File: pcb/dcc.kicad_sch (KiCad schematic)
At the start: 68 parts, among them U10 LM339, U11 LM339, U4 L78L05_SOT89, U5 L79L05_SOT89, U6 LM339, U7 LM339, U8 LM339, U9 4052

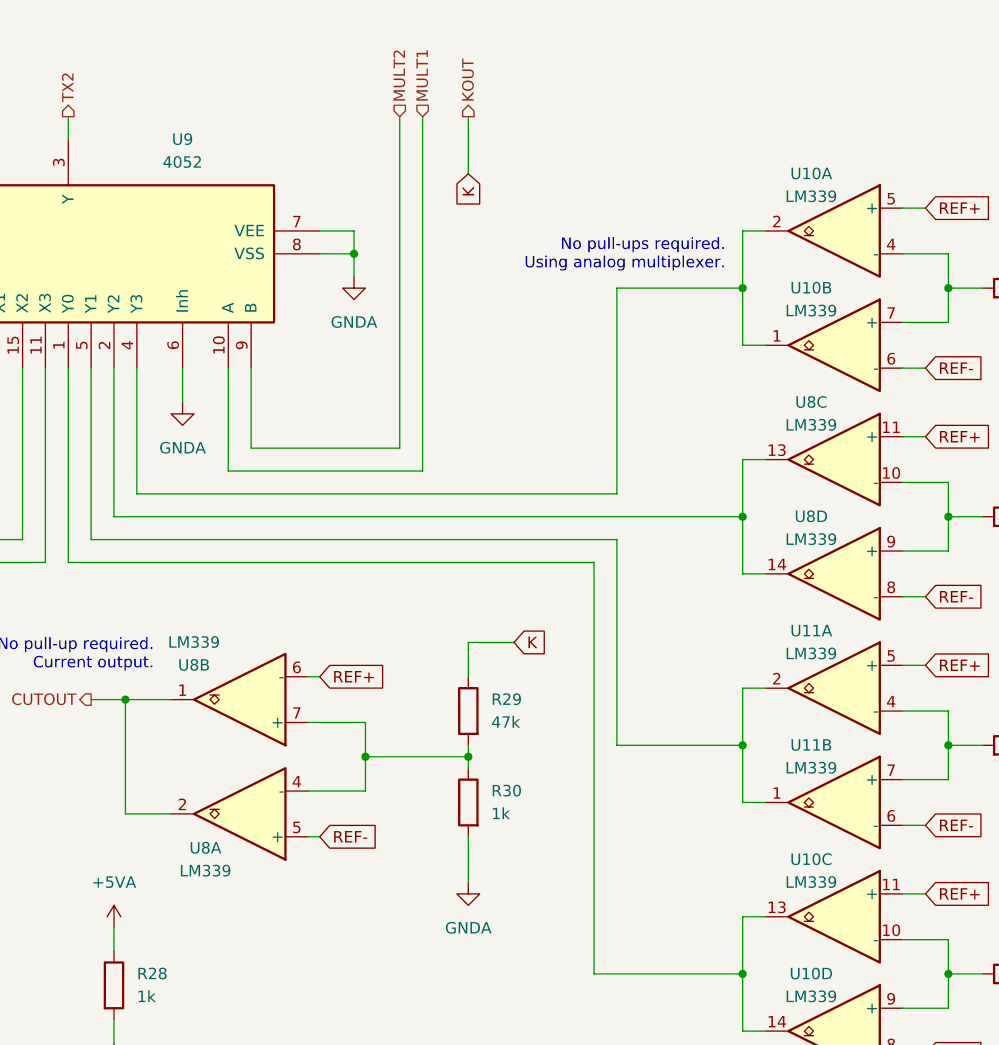
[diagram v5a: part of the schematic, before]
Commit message: pcb: wire multiplexors.
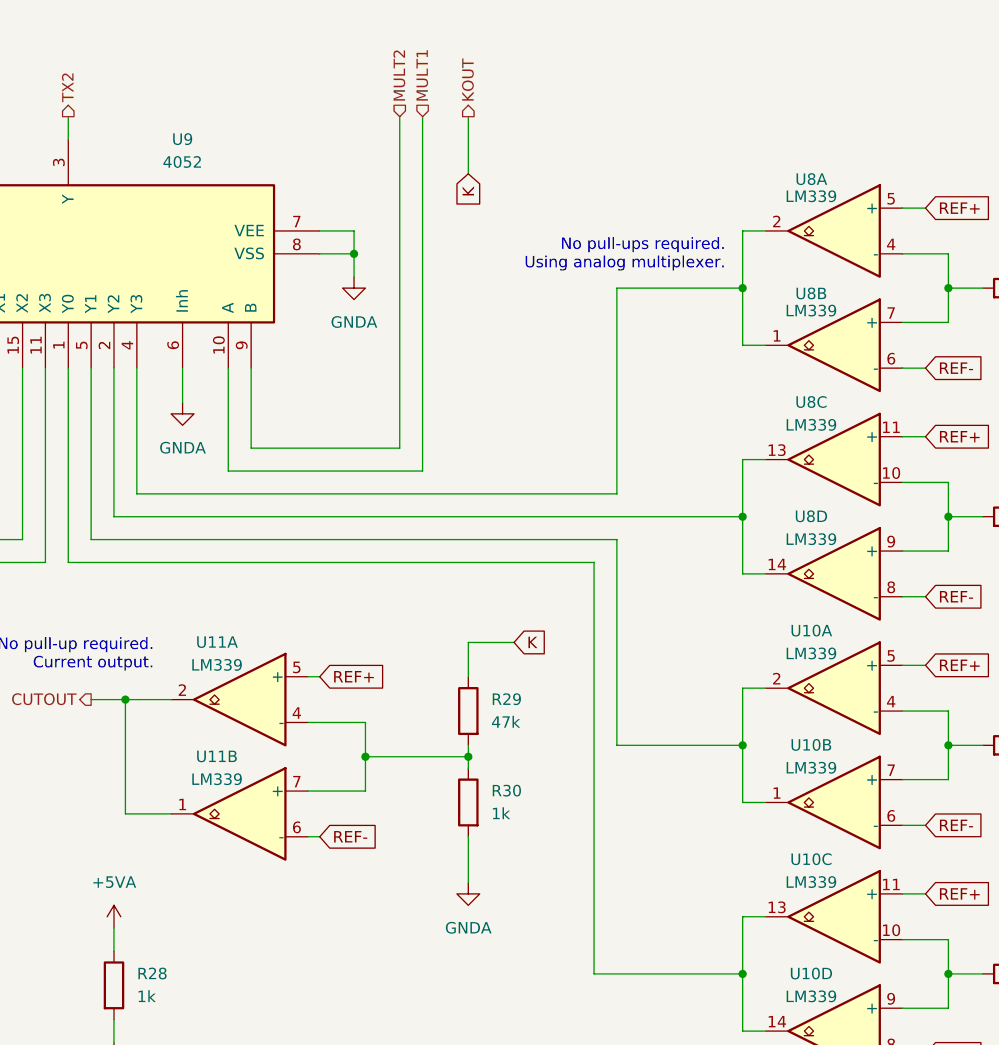
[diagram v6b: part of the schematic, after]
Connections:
- net CUTOUT: now also U11.1, U11.2; no longer U8.1, U8.2
- net REF+: now also U8.5 (+); no longer U8.6 (-)
- net REF-: now also U8.6 (-); no longer U8.5 (+)
- net at U10.1, U10.2: now also U9.5 (Y1); no longer U9.4 (Y3)
- net at U10.4 (-), U10.7 (+): now also R33.2; no longer R31.2
- net at U8.4 (-), U8.7 (+): now also R31.2; no longer R29.2, R30.1
- net at U11.4 (-), U11.7 (+): now also R29.2, R30.1; no longer R33.2
- new net: U8.1, U8.2, U9.4 (Y3)
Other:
- moved on the sheet: U10A, U10B, U11A, U11B, U8A, U8B
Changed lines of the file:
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@@
     )
   )
-  (symbol (lib_id "Comparator:LM339") (at 223.52 40.64 0) (mirror y) (unit 1)
-    (in_bom yes) (on_board yes) (dnp no)
-    (property "Reference" "U10" (at 220.98 34.29 0)
-      (effects (font (size 1.27 1.27)))
-    )
-    (property "Value" "LM339" (at 220.98 36.83 0)
-      (effects (font (size 1.27 1.27)))
-    )
-    (property "Footprint" "Package_SO:SO-14_3.9x8.65mm_P1.27mm" (at 224.79 38.1 0)
-      (effects (font (size 1.27 1.27)) hide)
-    )
-    (property "Datasheet" "https://www.st.com/resource/en/datasheet/lm139.pdf" (at 222.25 35.56 0)
+  (symbol (lib_id "Comparator:LM339") (at 223.52 91.44 0) (mirror y) (unit 1)
+    (in_bom yes) (on_board yes) (dnp no)
+    (property "Reference" "U10" (at 220.98 85.09 0)
+      (effects (font (size 1.27 1.27)))
+    )
+    (property "Value" "LM339" (at 220.98 87.63 0)
+      (effects (font (size 1.27 1.27)))
+    )
+    (property "Footprint" "Package_SO:SO-14_3.9x8.65mm_P1.27mm" (at 224.79 88.9 0)
+      (effects (font (size 1.27 1.27)) hide)
+    )
+    (property "Datasheet" "https://www.st.com/resource/en/datasheet/lm139.pdf" (at 222.25 86.36 0)
       (effects (font (size 1.27 1.27)) hide)
     )
@@
     )
   )
-  (symbol (lib_id "Comparator:LM339") (at 157.48 92.71 180) (unit 2)
-    (in_bom yes) (on_board yes) (dnp no)
-    (property "Reference" "U8" (at 152.4 88.9 0)
-      (effects (font (size 1.27 1.27)))
-    )
-    (property "Value" "LM339" (at 152.4 86.36 0)
-      (effects (font (size 1.27 1.27)))
-    )
-    (property "Footprint" "Package_SO:SO-14_3.9x8.65mm_P1.27mm" (at 158.75 95.25 0)
-      (effects (font (size 1.27 1.27)) hide)
-    )
-    (property "Datasheet" "https://www.st.com/resource/en/datasheet/lm139.pdf" (at 156.21 97.79 0)
+  (symbol (lib_id "Comparator:LM339") (at 223.52 53.34 0) (mirror y) (unit 2)
+    (in_bom yes) (on_board yes) (dnp no)
+    (property "Reference" "U8" (at 220.98 47.625 0)
+      (effects (font (size 1.27 1.27)))
+    )
+    (property "Value" "LM339" (at 220.98 49.53 0)
+      (effects (font (size 1.27 1.27)))
+    )
+    (property "Footprint" "Package_SO:SO-14_3.9x8.65mm_P1.27mm" (at 224.79 50.8 0)
+      (effects (font (size 1.27 1.27)) hide)
+    )
+    (property "Datasheet" "https://www.st.com/resource/en/datasheet/lm139.pdf" (at 222.25 48.26 0)
       (effects (font (size 1.27 1.27)) hide)
     )
@@
     )
   )
-  (symbol (lib_id "Comparator:LM339") (at 223.52 104.14 0) (mirror y) (unit 2)
-    (in_bom yes) (on_board yes) (dnp no)
-    (property "Reference" "U11" (at 220.98 97.79 0)
-      (effects (font (size 1.27 1.27)))
-    )
-    (property "Value" "LM339" (at 220.98 100.33 0)
-      (effects (font (size 1.27 1.27)))
-    )
-    (property "Footprint" "Package_SO:SO-14_3.9x8.65mm_P1.27mm" (at 224.79 101.6 0)
-      (effects (font (size 1.27 1.27)) hide)
-    )
-    (property "Datasheet" "https://www.st.com/resource/en/datasheet/lm139.pdf" (at 222.25 99.06 0)
+  (symbol (lib_id "Comparator:LM339") (at 157.48 105.41 0) (mirror y) (unit 2)
+    (in_bom yes) (on_board yes) (dnp no)
+    (property "Reference" "U11" (at 154.94 99.06 0)
+      (effects (font (size 1.27 1.27)))
+    )
+    (property "Value" "LM339" (at 154.94 101.6 0)
+      (effects (font (size 1.27 1.27)))
+    )
+    (property "Footprint" "Package_SO:SO-14_3.9x8.65mm_P1.27mm" (at 158.75 102.87 0)
+      (effects (font (size 1.27 1.27)) hide)
+    )
+    (property "Datasheet" "https://www.st.com/resource/en/datasheet/lm139.pdf" (at 156.21 100.33 0)
       (effects (font (size 1.27 1.27)) hide)
     )
@@
     )
   )
-  (symbol (lib_id "Comparator:LM339") (at 223.52 91.44 0) (mirror y) (unit 1)
-    (in_bom yes) (on_board yes) (dnp no)
-    (property "Reference" "U11" (at 220.98 85.09 0)
-      (effects (font (size 1.27 1.27)))
-    )
-    (property "Value" "LM339" (at 220.98 87.63 0)
-      (effects (font (size 1.27 1.27)))
-    )
-    (property "Footprint" "Package_SO:SO-14_3.9x8.65mm_P1.27mm" (at 224.79 88.9 0)
-      (effects (font (size 1.27 1.27)) hide)
-    )
-    (property "Datasheet" "https://www.st.com/resource/en/datasheet/lm139.pdf" (at 222.25 86.36 0)
+  (symbol (lib_id "Comparator:LM339") (at 157.48 92.71 0) (mirror y) (unit 1)
+    (in_bom yes) (on_board yes) (dnp no)
+    (property "Reference" "U11" (at 154.94 86.36 0)
+      (effects (font (size 1.27 1.27)))
+    )
+    (property "Value" "LM339" (at 154.94 88.9 0)
+      (effects (font (size 1.27 1.27)))
+    )
+    (property "Footprint" "Package_SO:SO-14_3.9x8.65mm_P1.27mm" (at 158.75 90.17 0)
+      (effects (font (size 1.27 1.27)) hide)
+    )
+    (property "Datasheet" "https://www.st.com/resource/en/datasheet/lm139.pdf" (at 156.21 87.63 0)
       (effects (font (size 1.27 1.27)) hide)
     )
@@
     )
   )
-  (symbol (lib_id "Comparator:LM339") (at 223.52 53.34 0) (mirror y) (unit 2)
-    (in_bom yes) (on_board yes) (dnp no)
-    (property "Reference" "U10" (at 220.98 46.99 0)
-      (effects (font (size 1.27 1.27)))
-    )
-    (property "Value" "LM339" (at 220.98 49.53 0)
-      (effects (font (size 1.27 1.27)))
-    )
-    (property "Footprint" "Package_SO:SO-14_3.9x8.65mm_P1.27mm" (at 224.79 50.8 0)
-      (effects (font (size 1.27 1.27)) hide)
-    )
-    (property "Datasheet" "https://www.st.com/resource/en/datasheet/lm139.pdf" (at 222.25 48.26 0)
+  (symbol (lib_id "Comparator:LM339") (at 223.52 104.14 0) (mirror y) (unit 2)
+    (in_bom yes) (on_board yes) (dnp no)
+    (property "Reference" "U10" (at 220.98 97.79 0)
+      (effects (font (size 1.27 1.27)))
+    )
+    (property "Value" "LM339" (at 220.98 100.33 0)
+      (effects (font (size 1.27 1.27)))
+    )
+    (property "Footprint" "Package_SO:SO-14_3.9x8.65mm_P1.27mm" (at 224.79 101.6 0)
+      (effects (font (size 1.27 1.27)) hide)
+    )
+    (property "Datasheet" "https://www.st.com/resource/en/datasheet/lm139.pdf" (at 222.25 99.06 0)
       (effects (font (size 1.27 1.27)) hide)
     )
@@
     )
   )
-  (symbol (lib_id "Comparator:LM339") (at 157.48 105.41 180) (unit 1)
-    (in_bom yes) (on_board yes) (dnp no)
-    (property "Reference" "U8" (at 153.67 109.22 0)
-      (effects (font (size 1.27 1.27)))
-    )
-    (property "Value" "LM339" (at 153.67 111.76 0)
-      (effects (font (size 1.27 1.27)))
-    )
-    (property "Footprint" "Package_SO:SO-14_3.9x8.65mm_P1.27mm" (at 158.75 107.95 0)
-      (effects (font (size 1.27 1.27)) hide)
-    )
-    (property "Datasheet" "https://www.st.com/resource/en/datasheet/lm139.pdf" (at 156.21 110.49 0)
-      (effects (font (size 1.27 1.27)) hide)
-    )
+  (symbol (lib_id "Comparator:LM339") (at 223.52 40.64 0) (mirror y) (unit 1)
+    (in_bom yes) (on_board yes) (dnp no)
+    (property "Reference" "U8" (at 220.98 34.925 0)
+      (effects (font (size 1.27 1.27)))
+    )
+    (property "Value" "LM339" (at 220.98 36.83 0)
+      (effects (font (size 1.27 1.27)))
+    )
+    (property "Footprint" "Package_SO:SO-14_3.9x8.65mm_P1.27mm" (at 224.79 38.1 0)
+      (effects (font (size 1.27 1.27)) hide)
+    )
+    (property "Datasheet" "https://www.st.com/resource/en/datasheet/lm139.pdf" (at 222.25 35.56 0)
+      (effects (font (size 1.27 1.27)) hide)
+    )
